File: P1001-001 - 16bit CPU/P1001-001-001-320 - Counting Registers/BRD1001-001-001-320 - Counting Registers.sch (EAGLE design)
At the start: 19 parts, among them IC1 74HC192D, IC12 74AC245DW, IC2 74HC192D, IC27 MEGA8535-A, IC3 74HC192D, IC4 74HC192D, IC7 74AC245DW, J1 22-27-2041-04

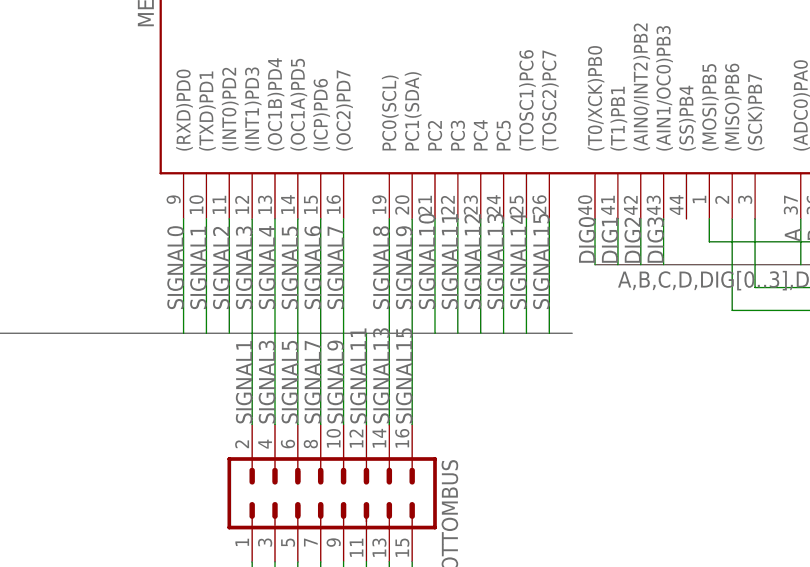
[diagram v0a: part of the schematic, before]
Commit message: add ram to Memory
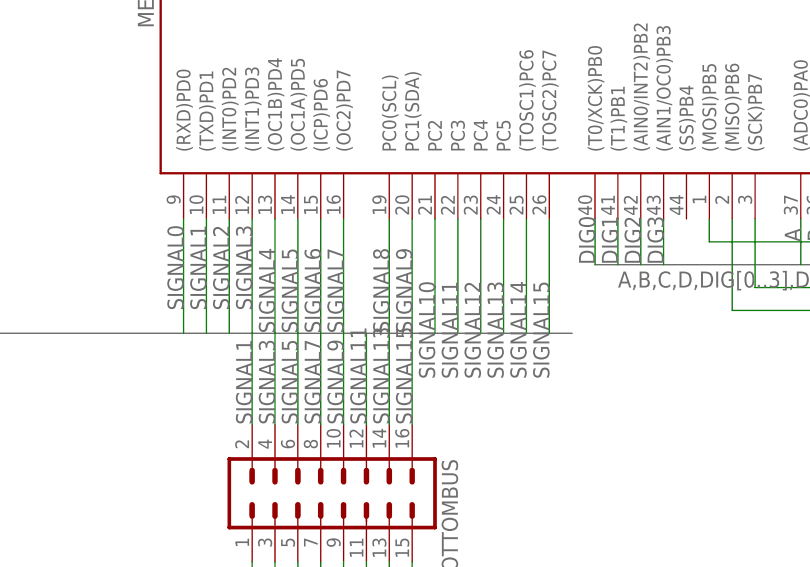
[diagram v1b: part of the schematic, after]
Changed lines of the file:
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@@
 <pinref part="IC27" gate="G$1" pin="(TOSC2)PC7"/>
 <wire x1="177.8" y1="-55.88" x2="177.8" y2="-68.58" width="0.1524" layer="91"/>
-<label x="177.8" y="-66.04" size="1.778" layer="95" rot="R90"/>
+<label x="177.8" y="-73.66" size="1.778" layer="95" rot="R90"/>
 </segment>
 <segment>
@@
 <pinref part="IC27" gate="G$1" pin="(TOSC1)PC6"/>
 <wire x1="175.26" y1="-55.88" x2="175.26" y2="-68.58" width="0.1524" layer="91"/>
-<label x="175.26" y="-66.04" size="1.778" layer="95" rot="R90"/>
+<label x="175.26" y="-73.66" size="1.778" layer="95" rot="R90"/>
 </segment>
 <segment>
@@
 <pinref part="IC27" gate="G$1" pin="PC5"/>
 <wire x1="172.72" y1="-55.88" x2="172.72" y2="-68.58" width="0.1524" layer="91"/>
-<label x="172.72" y="-66.04" size="1.778" layer="95" rot="R90"/>
+<label x="172.72" y="-73.66" size="1.778" layer="95" rot="R90"/>
 </segment>
 <segment>
@@
 <pinref part="IC27" gate="G$1" pin="PC4"/>
 <wire x1="170.18" y1="-55.88" x2="170.18" y2="-68.58" width="0.1524" layer="91"/>
-<label x="170.18" y="-66.04" size="1.778" layer="95" rot="R90"/>
+<label x="170.18" y="-73.66" size="1.778" layer="95" rot="R90"/>
 </segment>
 <segment>
@@
 <pinref part="IC27" gate="G$1" pin="PC3"/>
 <wire x1="167.64" y1="-55.88" x2="167.64" y2="-68.58" width="0.1524" layer="91"/>
-<label x="167.64" y="-66.04" size="1.778" layer="95" rot="R90"/>
+<label x="167.64" y="-73.66" size="1.778" layer="95" rot="R90"/>
 </segment>
 <segment>
@@
 <pinref part="IC27" gate="G$1" pin="PC2"/>
 <wire x1="165.1" y1="-55.88" x2="165.1" y2="-68.58" width="0.1524" layer="91"/>
-<label x="165.1" y="-66.04" size="1.778" layer="95" rot="R90"/>
+<label x="165.1" y="-73.66" size="1.778" layer="95" rot="R90"/>
 </segment>
 <segment>
@@
 <pinref part="IC27" gate="G$1" pin="PC1(SDA)"/>
 <wire x1="162.56" y1="-55.88" x2="162.56" y2="-68.58" width="0.1524" layer="91"/>
-<label x="162.56" y="-66.04" size="1.778" layer="95" rot="R90"/>
+<label x="162.56" y="-68.58" size="1.778" layer="95" rot="R90"/>
 </segment>
 <segment>
@@
 <pinref part="IC27" gate="G$1" pin="PC0(SCL)"/>
 <wire x1="160.02" y1="-55.88" x2="160.02" y2="-68.58" width="0.1524" layer="91"/>
-<label x="160.02" y="-66.04" size="1.778" layer="95" rot="R90"/>
+<label x="160.02" y="-68.58" size="1.778" layer="95" rot="R90"/>
 </segment>
 <segment>
@@
 <pinref part="IC27" gate="G$1" pin="(OC2)PD7"/>
 <wire x1="154.94" y1="-55.88" x2="154.94" y2="-68.58" width="0.1524" layer="91"/>
-<label x="154.94" y="-66.04" size="1.778" layer="95" rot="R90"/>
+<label x="154.94" y="-68.58" size="1.778" layer="95" rot="R90"/>
 </segment>
 <segment>
@@
 <pinref part="IC27" gate="G$1" pin="(ICP)PD6"/>
 <wire x1="152.4" y1="-55.88" x2="152.4" y2="-68.58" width="0.1524" layer="91"/>
-<label x="152.4" y="-66.04" size="1.778" layer="95" rot="R90"/>
+<label x="152.4" y="-68.58" size="1.778" layer="95" rot="R90"/>
 </segment>
 <segment>
@@
 <pinref part="IC27" gate="G$1" pin="(OC1B)PD4"/>
 <wire x1="147.32" y1="-55.88" x2="147.32" y2="-68.58" width="0.1524" layer="91"/>
-<label x="147.32" y="-66.04" size="1.778" layer="95" rot="R90"/>
+<label x="147.32" y="-68.58" size="1.778" layer="95" rot="R90"/>
 </segment>
 <segment>
@@
 <pinref part="IC27" gate="G$1" pin="(OC1A)PD5"/>
 <wire x1="149.86" y1="-55.88" x2="149.86" y2="-68.58" width="0.1524" layer="91"/>
-<label x="149.86" y="-66.04" size="1.778" layer="95" rot="R90"/>
-</segment>
-<segment>
+<label x="149.86" y="-68.58" size="1.778" layer="95" rot="R90"/>
+</segment>
+<segment>
